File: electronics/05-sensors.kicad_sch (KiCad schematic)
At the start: 24 parts, among them Q501 AO3400A, Q502 BPW77NA, U501 VL53L1CBV0FY/1, U502 VL53L1CBV0FY/1, U503 LSM6DSOTR

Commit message: Passe le microcontrôleur en LQFP144 et lit les deux courants au même instant
Le LQFP100 avait ses seize entrées ADC prises — douze voies de ligne, trois
de télémétrie, une sortie de multiplexeur — et c'est ce multiplexeur qui
posait le vrai problème : il interdisait par construction de lire les deux
courants moteur ensemble. On lisait un moteur, on commutait, on attendait
l'établissement, on lisait l'autre. Le STM32H723ZGT6 en LQFP144 place
PF11 sur ADC1_INP2 et PF13 sur ADC2_INP2 : même numéro de voie sur deux
convertisseurs, donc une lecture simultanée en mode double, et le 74HC4051
disparaît de la carte.

Le brochage étant donné par nom de port et non par numéro de broche, le
passage a coûté deux affectations sur quatre-vingt-sept. Une affectation est
un choix de port — PA0 porte la voie de ligne 00 — jamais un choix de patte.
Une table numérotée aurait demandé de recopier 144 lignes à la main, et une
erreur de brochage ne se voit pas à l'ERC.

Ajoute une huitième feuille, les témoins de ligne. Ce qu'on regarde pendant
un essai n'est pas un témoin d'état générique, c'est ce que voit la
moustache : une LED par capteur, à l'aplomb du capteur qu'elle rapporte, et
un capteur borgne se voit avant la course plutôt qu'après. Le rapport
cyclique suit le signal, sinon rien ne dirait si la ligne est au bord ou au
centre du trait. PCA9685 à l'adresse 0x40 sur I²C2, 52 octets par rafale
soit 1,2 ms à 400 kHz, en DMA hors de la boucle rapide.

Remplace l'interrupteur à glissière par une mise sous tension à bouton
poussoir : une impulsion amorce, le microcontrôleur se tient lui-même, et
c'est lui qui coupe. La glissière demandait une place au bord de carte que
le pack, l'équilibrage et les fils de l'ESC ont fini par prendre — et elle
ne savait pas éteindre proprement, couper le 3,3 V sous les pieds du
firmware n'ayant jamais rien écrit dans la flash.

Ajoute au générateur le contrôle qui manquait : deux extrémités de nets
différents au même point. Il a fallu qu'il relie B+ à B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
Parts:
- removed C506: 100nF, Capacitor_SMD:C_0603_1608Metric, symbol Device:C
- removed C507: 1nF, Capacitor_SMD:C_0603_1608Metric, symbol Device:C
- removed D501: OPV302 - laser IR 850 nm, Package_TO_SOT_THT:TO-18-2, symbol Device:LED
- removed Q502: BPW77NA, Package_TO_SOT_THT:TO-18-2, symbol Device:Q_Photo_NPN
- removed R509: 100k, Resistor_SMD:R_0603_1608Metric, symbol Device:R
- removed R510: 47k, Resistor_SMD:R_0603_1608Metric, symbol Device:R
- removed R511: 1k, Resistor_SMD:R_0603_1608Metric, symbol Device:R
- added C521, C541: 22pF, Capacitor_SMD:C_0402_1005Metric, symbol Device:C
- added C522, C542: 1nF, Capacitor_SMD:C_0402_1005Metric, symbol Device:C
- added C523, C543, C561, C562: 1uF, Capacitor_SMD:C_0402_1005Metric, symbol Device:C
- added C524, C544: 4n7, Capacitor_SMD:C_0402_1005Metric, symbol Device:C
- added C525, C545: 10nF, Capacitor_SMD:C_0402_1005Metric, symbol Device:C
- added C563, C564, C566, C567, C568: 100nF, Capacitor_SMD:C_0402_1005Metric, symbol Device:C
- added C565: 10uF, Capacitor_SMD:C_0805_2012Metric, symbol Device:C
- added D503, D523, D543: PESD3V3, Diode_SMD:D_SOD-323, symbol Device:D_TVS
- added D504, D524, D544: BAT54, Diode_SMD:D_SOD-323, symbol Device:D_Schottky
- added Q521, Q541: AO3400A, Package_TO_SOT_SMD:SOT-23, symbol Transistor_FET:AO3400A
- added R521, R522, R541, R542: 100R, Resistor_SMD:R_0402_1005Metric, symbol Device:R
- added R523, R525, R526, R543, R545, R546: 100k, Resistor_SMD:R_0402_1005Metric, symbol Device:R
- added R524, R544: 220k, Resistor_SMD:R_0402_1005Metric, symbol Device:R
- added R527, R547: 910R, Resistor_SMD:R_0402_1005Metric, symbol Device:R
- added R528, R548: 1k, Resistor_SMD:R_0402_1005Metric, symbol Device:R
- added R561, R563, R564: 10k, Resistor_SMD:R_0402_1005Metric, symbol Device:R
- added R562: 2k2, Resistor_SMD:R_0402_1005Metric, symbol Device:R
- added TM501, TM521, TM541: OPV302 + BPV10NF, Pacabot:Telemetry_Duo_Coude, symbol Pacabot:Telemetry_Duo
- added unit 2 of U501
- added unit 3 of U501
- added unit 4 of U501
- added unit 5 of U501
- added unit 5 of U502
- added unit 4 of U502
- added unit 2 of U502
- added unit 3 of U502
- added U504: TLV9064, Package_SO:TSSOP-14_4.4x5mm_P0.65mm, symbol Amplifier_Operational:TLV9064
- C501: value 100nF -> 22pF; footprint Capacitor_SMD:C_0603_1608Metric -> Capacitor_SMD:C_0402_1005Metric; Dielectric (none) -> C0G; Voltage (none) -> 50V
- C502: value 4u7F -> 1nF; footprint Capacitor_SMD:C_0805_2012Metric -> Capacitor_SMD:C_0402_1005Metric; Dielectric (none) -> X7R; Voltage (none) -> 25V
- C503: value 100nF -> 1uF; footprint Capacitor_SMD:C_0603_1608Metric -> Capacitor_SMD:C_0402_1005Metric; Dielectric (none) -> X5R; Voltage (none) -> 16V
- C504: value 4u7F -> 4n7; footprint Capacitor_SMD:C_0805_2012Metric -> Capacitor_SMD:C_0402_1005Metric; Dielectric (none) -> X7R; Voltage (none) -> 25V
- C505: value 100nF -> 10nF; footprint Capacitor_SMD:C_0603_1608Metric -> Capacitor_SMD:C_0402_1005Metric
- R501, R502: value 10k -> 100R; footprint Resistor_SMD:R_0603_1608Metric -> Resistor_SMD:R_0402_1005Metric; Power (none) -> 63mW
- R503: value 10k -> 100k; footprint Resistor_SMD:R_0603_1608Metric -> Resistor_SMD:R_0402_1005Metric; Power (none) -> 63mW
- R504: value 10k -> 220k; footprint Resistor_SMD:R_0603_1608Metric -> Resistor_SMD:R_0402_1005Metric; Power (none) -> 63mW
- R505, R506: value 2k2 -> 100k; footprint Resistor_SMD:R_0603_1608Metric -> Resistor_SMD:R_0402_1005Metric; Power (none) -> 63mW
- R507: value 15R -> 910R; footprint Resistor_SMD:R_0603_1608Metric -> Resistor_SMD:R_0402_1005Metric; Power (none) -> 63mW
- R508: value 100R -> 1k; footprint Resistor_SMD:R_0603_1608Metric -> Resistor_SMD:R_0402_1005Metric; Power (none) -> 63mW
- U501, U502: value VL53L1CBV0FY/1 -> TLV9064; footprint Sensor_Distance:ST_VL53L1x -> Package_SO:TSSOP-14_4.4x5mm_P0.65mm; symbol Sensor_Distance:VL53L1CXV0FY1 -> Amplifier_Operational:TLV9064; LCSC C2970716 -> (none)
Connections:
- net +3V3: now also C566.1, C567.1, R521.1, R541.1; no longer C501.1, C502.1, C503.1, C504.1, C505.1, R502.1, R503.1, R504.1, R505.1, R506.1, R507.1, U501.1 (AVDDVCSEL), U501.11 (AVDD), U502.1 (AVDDVCSEL), U502.11 (AVDD)
- net +3V3A: now also C563.1, C564.1, C565.1, C568.1, R561.1, R563.1, TM501.3 (RX_K), TM521.3 (RX_K), TM541.3 (RX_K), U501.4 (V+), U502.4 (V+), U504.4 (V+)
- net GND: now also R503.2, C523.2, C524.2, C543.2, C544.2, C561.2, C562.2, C563.2, C564.2, C565.2, C566.2, C567.2, C568.2, D503.2 (A2), D504.2 (A), D523.2 (A2), D524.2 (A), D543.2 (A2), D544.2 (A), Q521.2 (S), Q541.2 (S), R523.2, R543.2, R562.2, R564.2, U501.11 (V-), U502.11 (V-), U504.11 (V-); no longer C501.2, C502.2, C505.2, U501.12 (GND), U501.2 (AVSSVCSEL), U501.3 (GND), U501.4 (GND), U501.6 (GND), U502.12 (GND), U502.2 (AVSSVCSEL), U502.3 (GND), U502.4 (GND), U502.6 (GND)
- net Q501_G: now also R502.2, R503.1; no longer R508.2
- net IR_LASER_EN renamed AMP_F
- net AMP_F: now also R506.1, U501.7
- net LASER_A renamed CG_F
- net CG_F: now also C503.1
- net LASER_K renamed LAS_F_K
- net LAS_F_K: now also D503.1 (A1), TM501.1 (TX_K)
- removed net SCL1: R506.2, U501.10 (SCL), U502.10 (SCL)
- removed net SDA1: R505.2, U501.9 (SDA), U502.9 (SDA)
- net TOF_FL_INT renamed TIA_F
- net TIA_F: now also C501.2, C502.1, U501.1; no longer U502.7 (GPIO1)
- removed net TOF_FL_XSHUT: R503.2, U502.5 (XSHUT)
- removed net TOF_F_INT: R502.2, U501.7 (GPIO1)
- net TOF_F_XSHUT renamed LAS_F_A
- net LAS_F_A: now also TM501.2 (TX_A); no longer U501.5 (XSHUT)
- new net AMP_FL: R526.1, R528.1, U502.7
- new net AMP_L: R546.1, R548.1, U504.7
- new net CG_FL: C523.1, R527.2
- new net CG_L: C543.1, R547.2
- new net FB_F: R506.2, R507.1, U501.6 (-)
- new net FB_FL: R526.2, R527.1, U502.6 (-)
- new net FB_L: R546.2, R547.1, U504.6 (-)
- new net G_F: C502.2, R505.1, U501.5 (+)
- new net G_FL: C522.2, R525.1, U502.5 (+)
- new net G_L: C542.2, R545.1, U504.5 (+)
- new net LAS_FL_A: R521.2, TM521.2 (TX_A)
- new net LAS_FL_K: D523.1 (A1), Q521.3 (D), TM521.1 (TX_K)
- new net LAS_L_A: R541.2, TM541.2 (TX_A)
- new net LAS_L_K: D543.1 (A1), Q541.3 (D), TM541.1 (TX_K)
- new net PD_F: C501.1, R504.1, TM501.4 (RX_A), U501.2 (-)
- new net PD_FL: C521.1, R524.1, TM521.4 (RX_A), U502.2 (-)
- new net PD_L: C541.1, R544.1, TM541.4 (RX_A), U504.2 (-)
- new net Q521_G: Q521.1 (G), R522.2, R523.1
- new net Q541_G: Q541.1 (G), R542.2, R543.1
- new net RX_F: C504.1, R508.2
- new net RX_FL: C524.1, R528.2
- new net RX_L: C544.1, R548.2
- new net TIA_FL: C521.2, C522.1, R524.2, U502.1
- new net TIA_L: C541.2, C542.1, R544.2, U504.1
- new net TXAC_F: C505.2, D504.1 (K), R502.1
- new net TXAC_FL: C525.2, D524.1 (K), R522.1
- new net TXAC_L: C545.2, D544.1 (K), R542.1
- new net TX_F: C505.1
- new net TX_FL: C525.1
- new net TX_L: C545.1
- new net U501_SPARE_3: U501.8, U501.9 (-)
- new net U502_SPARE: U502.13 (-), U502.14
- new net U502_SPARE_3: U502.8, U502.9 (-)
- new net U504_SPARE_3: U504.8, U504.9 (-)
- new net U504_SPARE_4: U504.13 (-), U504.14
- new net VREF_MID: R505.2, R525.2, R545.2, U501.13 (-), U501.14
- new net VREF_MID_R: C562.1, R563.2, R564.1, U501.12 (+)
- new net VREF_RX: C561.1, R561.2, R562.1, U501.10 (+), U501.3 (+), U502.10 (+), U502.12 (+), U502.3 (+), U504.10 (+), U504.12 (+), U504.3 (+)
- no-connect marks 5 -> 3
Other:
- note added: "C563 / C564 / C568 : 100 nF local, broche 4 vers masse. Entrees inutilisees polarisees par VREF_RX, sorties bouclees. Plan de masse continu ; retours TX eloignes des noeuds PD."
- note added: "Emission codee, couplage alternatif avant le gain, demodulation I/Q dans le firmware : le gain de traitement vient du retrecissement de bande, pas de l optique."
- note added: "Implantation locale des trois chaines analogiques"
- note added: "References et alimentation des amplificateurs"
- note added: "SDX et SCX a la masse : bus auxiliaire inutilise. A implanter au centre de rotation, pres de l essieu."
- note added: "Station F - avant, 15 deg"
- note added: "Station FL - avant-gauche, 45 deg"
- note added: "Station L - gauche, 75 deg"
- note added: "U501 : F ; U502 : FL ; U504 : L. A = TIA, B = gain, dans chaque boitier. R/C de contre-reaction au ras des broches 1/2 et 6/7. R508/C504, R528/C524 et R548/C544 au pied des ADC. Aucune longue liaison de photodiode entre stations."
- note removed: "Composants nus reflowes par JLCPCB, pas de modules tout faits : c est l orientation qui compte, et elle doit etre gravee dans le cuivre. Mode long, budget 20 ms -> 50 Hz, soit 6 cm entre deux mesures a 3 m/s."
- note removed: "Lu a chaque conversion ADC, donc a 1 kHz, la ou un VL53L1X plafonne a 50 Hz. Calibration en intensite contre le vrai mur pendant les essais libres. Approvisionnement OPV302 / BPW77 a confirmer : pose manuelle sur une carte par ailleurs assemblee, ou repli sur un VL53L1X. Empreintes TO-18 a recaler sur le boitier reellement recu."
- note removed: "SDX et SCX a la masse : le bus auxiliaire n est pas utilise. A implanter au centre de rotation, pres de l essieu moteur."
- note removed: "Telemetre ToF avant, 0 deg"
- note removed: "Telemetre ToF avant-gauche, 45 deg"
- note removed: "Telemetre analogique lateral gauche - mur de la Q1"
- note removed: "Tirage unique du bus I2C1, cote carte mere."
- title: UsainBot - Telemetrie ToF, voie analogique rapide, inertie -> UsainBot - Telemetrie analogique a detection synchrone, inertie
- moved on the sheet: C501, C502, C503, C504, C505, Q501, R501, R502, R503, R504, R505, R506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

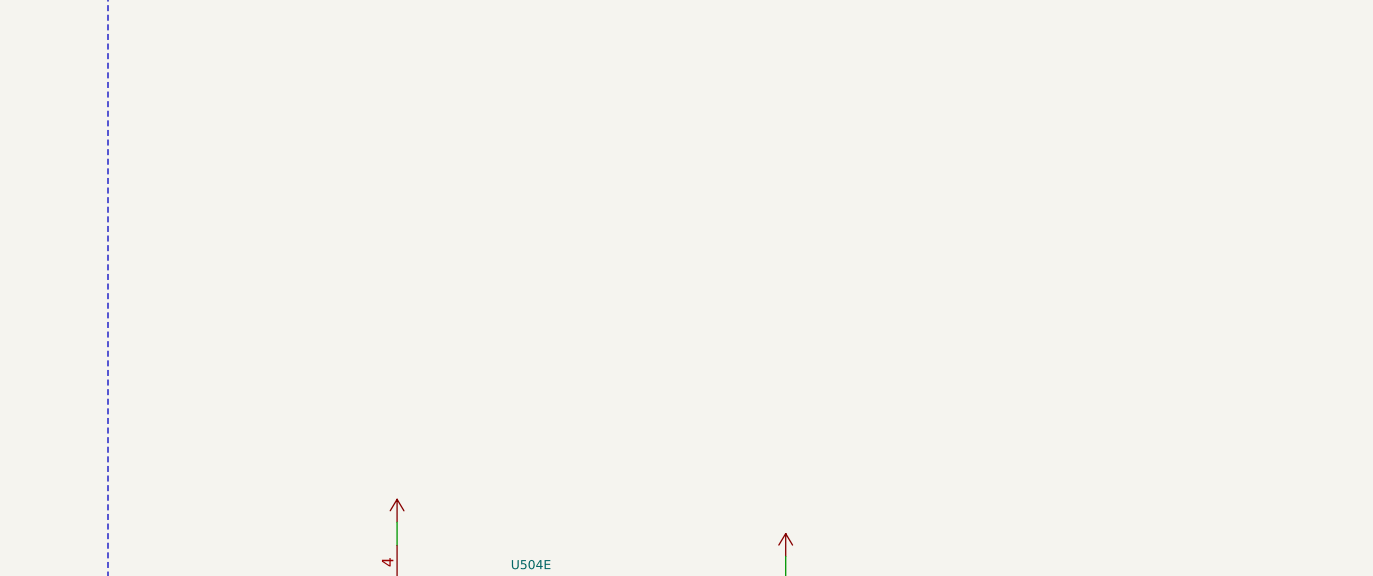
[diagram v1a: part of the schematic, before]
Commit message: Replace la carte autour de ses chaînes analogiques et y intègre le pack commun et l'ESC
Le placement du 4 septembre rangeait les pièces par zone. Celui-ci part des
nets et des vraies pastilles, et affecte chaque condensateur à une broche
plutôt qu'à une couronne autour du boîtier. Le STM32 pivote de 180° sur son
centre pour tourner son côté analogique vers la barrette. Chaque station
laser reçoit son propre TLV9064 (U504 s'ajoute pour la station L), et la
liaison photodiode → TIA tombe de 34, 56 et 69 mm à 3,1, 7,4 et 2,9 mm. La
boucle de retour du TIA passe de 140–150 mm à 3,55. Cinq découplages
suivent : C568, C569/C570 sur VREF_RX, C223/C224 sur VBAT du MCU et C351
sur VREF_MOT du pont droit.

`layout.py`, `layout_fit.json` et `place_pcb.py --reset` ne décrivent plus
cette carte. Le README le dit en tête, et les nouveaux outils partent du
PCB courant, jamais de l'ancienne table. `audit_placement_geometry.py` relit
les courtyards orientés et les contrôle sous Shapely, `placement_metrics.py`
et `preview_analog_paths.py` mesurent distances et couloirs sans poser une
piste. `refine_placement.py` calcule la table, `apply_refined_placement.py`
l'écrit en vérifiant verrous et UUID : il ne se rejoue pas après une
retouche à la main.

L'alimentation change de nature. Le pack LiFePO4 et son ESC sur VBAT
laissent place à un pack 2S commun, chimie encore à choisir, que la carte,
les moteurs et la turbine partagent. Une seule prise MR30 à trois contacts
porte GND, point milieu et VPACK, et remplace XT30 + JST-XH. L'ESC devient
un EMAX Bullet 12A (12 A continu, 15 A crête, sans BEC) sur VPACK brut,
monté debout sur J103. J104 et J702 disparaissent. ESC103 et M703 sont des
symboles hors carte : les phases moteur ne reçoivent aucun pad fictif, et
le module ne compte qu'une fois dans la nomenclature. R107 passe de 10 à
47 Ω pour ramener l'équilibrage à 88 mA et 0,36 W, sous le watt de son
boîtier 2512. La recharge reste inhibée par défaut matériel tant que
cellules, profil et fir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
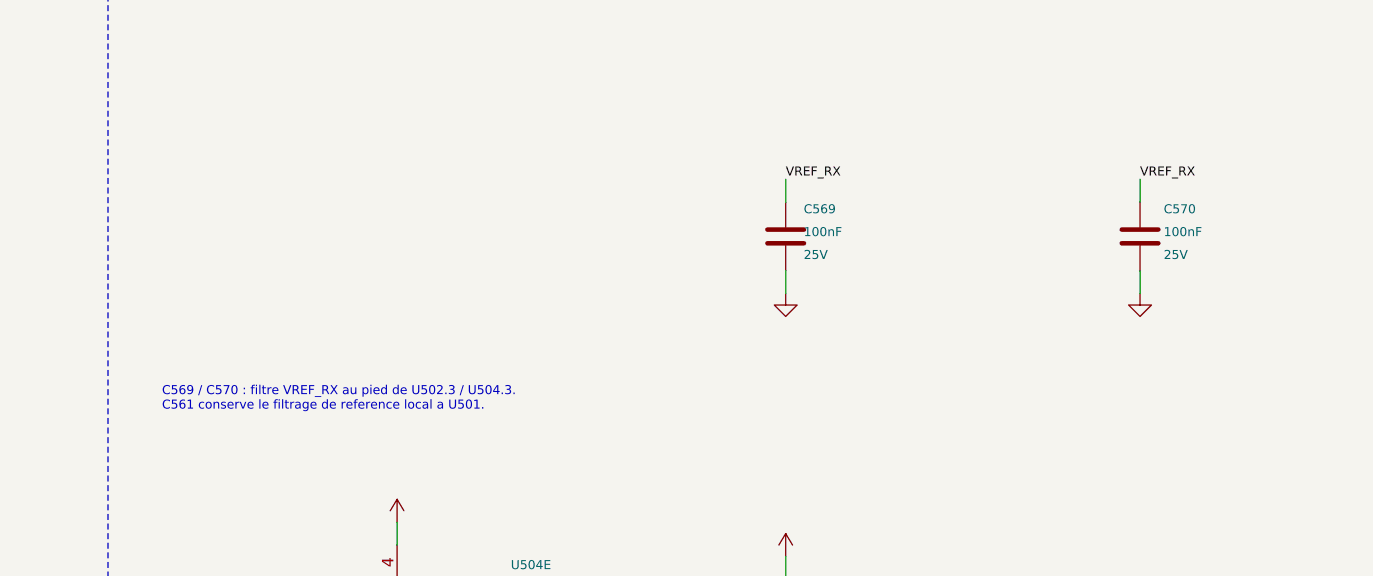
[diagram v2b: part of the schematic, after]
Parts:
- added C569, C570: 100nF, Capacitor_SMD:C_0402_1005Metric, symbol Device:C
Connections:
- net GND: now also C569.2, C570.2
- net VREF_RX: now also C569.1, C570.1
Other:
- note added: "C569 / C570 : filtre VREF_RX au pied de U502.3 / U504.3. C561 conserve le filtrage de reference local a U501."
